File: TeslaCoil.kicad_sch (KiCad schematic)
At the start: 12 parts, among them J1 USB_B_Micro, J2 Conn_01x06_Pin, SW1 SW_DPDT_x2, U1 ATtiny25-20S

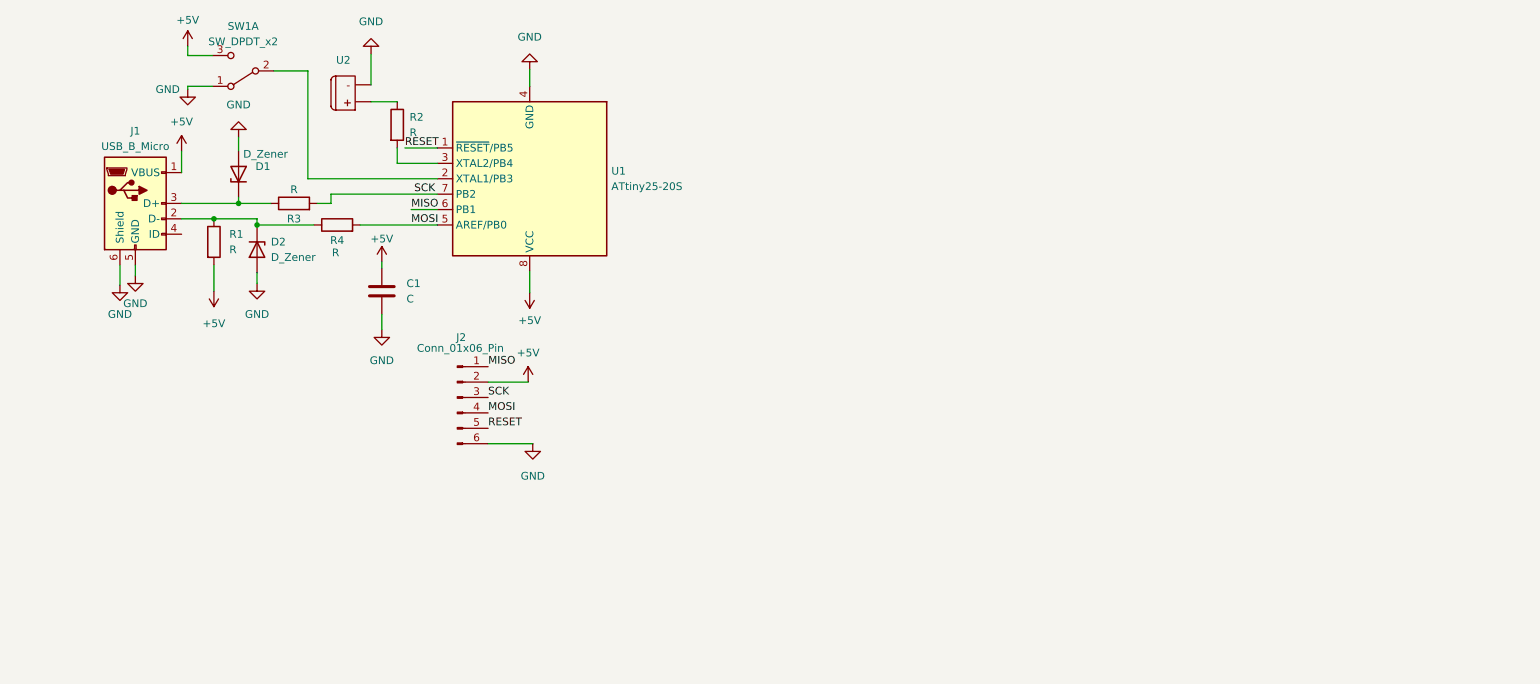
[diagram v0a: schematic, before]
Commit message: Added gitignore, removed backups from version control
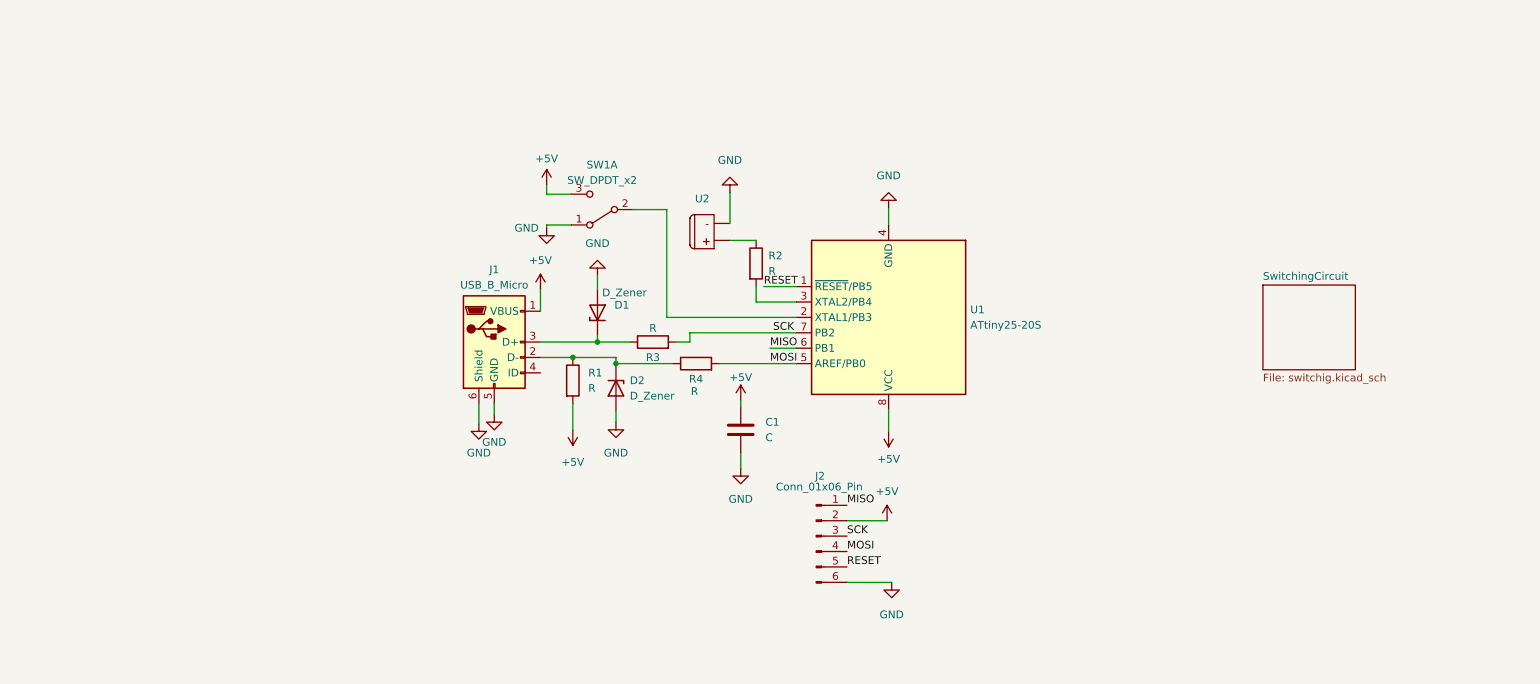
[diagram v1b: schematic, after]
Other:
- added sheet SwitchingCircuit (switchig.kicad_sch)
- company: (none) -> UN Sede Manizales
- title: (none) -> USB Interrupter
- moved on the sheet: C1, D1, D2, J1, J2, R1, R2, R3, R4, SW1A, U1, U2

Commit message: footprints added
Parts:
- C1: value C -> 1u; footprint (none) -> Capacitor_SMD:C_1206_3216Metric
- D1, D2: footprint (none) -> Diode_SMD:D_0603_1608Metric
- R1: value R -> 1.5k; footprint (none) -> Resistor_SMD:R_0402_1005Metric
- R2: value R -> 100; footprint (none) -> Resistor_SMD:R_0402_1005Metric
- R3, R4: value R -> 68; footprint (none) -> Resistor_SMD:R_0402_1005Metric
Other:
- moved on the sheet: D2, J2, R2, R4

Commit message: New project
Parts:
- removed C1: 1u, Capacitor_SMD:C_1206_3216Metric, symbol Device:C
- removed D1, D2: D_Zener, Diode_SMD:D_0603_1608Metric, symbol Device:D_Zener
- removed J1: USB_B_Micro, Connector_USB:USB_Micro-B_Molex-105017-0001, symbol Connector:USB_B_Micro
- removed J2: Conn_01x06_Pin, Connector_PinHeader_1.00mm:PinHeader_2x03_P1.00mm_Vertical, symbol Connector:Conn_01x06_Pin
- removed R1: 1.5k, Resistor_SMD:R_0402_1005Metric, symbol Device:R
- removed R2: 100, Resistor_SMD:R_0402_1005Metric, symbol Device:R
- removed R3, R4: 68, Resistor_SMD:R_0402_1005Metric, symbol Device:R
- removed SW1: SW_DPDT_x2, symbol Switch:SW_DPDT_x2
- removed U1: ATtiny25-20S, Package_SO:SOIC-8W_5.3x5.3mm_P1.27mm, symbol MCU_Microchip_ATtiny:ATtiny25-20S
- removed U2: ~, symbol FibreOpticTransmitterJack:FibreOpticTransmitterJack

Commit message: PCB teslacoil
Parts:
- added C1, C2, C3, C4: 1u, Capacitor_SMD:C_1206_3216Metric, symbol Device:C
- added C5, C6, C9: 100u, Capacitor_SMD:C_1206_3216Metric, symbol Device:C_Polarized_US
- added C7, C8: 47u, Capacitor_THT:CP_Radial_D10.0mm_P5.00mm, symbol Device:C_Polarized_US
- added D1, D2: D, Diode_SMD:D_0603_1608Metric, symbol Device:D
- added D3: DF005s, Diode_THT:Diode_Bridge_DIP-4_W7.62mm_P5.08mm, symbol Diode_Bridge:DF005M
- added D4: DF206S-G, Diode_THT:Diode_Bridge_DIP-4_W7.62mm_P5.08mm, symbol Diode_Bridge:DF005M
- added F1: 4A, Fuse:Fuseholder_Clip-6.3x32mm_Littelfuse_102_122_Inline_P34.21x7.62mm_D1.98mm_Horizontal, symbol Device:Fuse
- added J1: Conn_01x03_Pin, Connector_PinHeader_2.54mm:PinHeader_1x03_P2.54mm_Horizontal, symbol Connector:Conn_01x03_Pin
- added J2: Conn_02x02_Counter_Clockwise, Connector_PinHeader_1.00mm:PinHeader_2x02_P1.00mm_Vertical, symbol Connector_Generic:Conn_02x02_Counter_Clockwise
- added J3: Conn_01x03_Pin, Connector_PinHeader_1.00mm:PinHeader_1x03_P1.00mm_Vertical, symbol Connector:Conn_01x03_Pin
- added Q1, Q2: ~, Package_TO_SOT_THT:TO-220-3_Vertical, symbol TeslaCoil:STGB19NC60KDT4
- added R1: 4.7, Resistor_SMD:R_0402_1005Metric, symbol Device:R_US
- added R2: 100K, Resistor_SMD:R_0402_1005Metric, symbol Device:R_US
- added R3: 100k, Resistor_SMD:R_0402_1005Metric, symbol Device:R_US
- added T1: Transformer_1P_1S, TeslaCoil_JDG:AS3010-U-0100-120-S, symbol Device:Transformer_1P_1S
- added T2: ~, TeslaCoil_JDG:PA2002NL, symbol TeslaCoil:PA2002NL
- added U1: ~, TeslaCoil_JDG:SN74LVC2G14-Q1, symbol TeslaCoil:SN74LVC2G14-Q1
- added U2: ~, TeslaCoil_JDG:IF-D95T, symbol TeslaCoil:IF-D95T
- added U3: ~, TeslaCoil_JDG:UCC27425, symbol TeslaCoil:UCC27425
- added U4: 7815L, TeslaCoil_JDG:L7805ABD2T-TR, symbol Regulator_Linear:L7815
- added U5: 78L05Z, TeslaCoil_JDG:L7805ABD2T-TR, symbol Regulator_Linear:L7815
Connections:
- new net: C4.1, U3.7 (OUTA)
- new net: C4.2, J2.3 (Pin_3)
- new net: D3.3, T1.3 (SA)
- new net: D3.4, T1.4 (SB)
- new net: C7.1, D4.1 (+), Q1.2, R2.1
- new net: C7.2, C8.1, J3.3 (Pin_3), R2.2, R3.1
- new net: U2.2 (OUT), U3.1 (ENBA), U3.8 (ENBB)
- new net: U1.4 (2Y), U3.2 (INA), U3.4 (INB)
- new net: R1.1, U3.5 (OUTB)
- new net: J2.1 (Pin_1), R1.2
- new net: J2.2 (Pin_2), T2.8
- new net: J2.4 (Pin_4), T2.1
- new net: J3.1 (Pin_1), Q1.3, Q2.2, T2.3
- new net: Q2.1, T2.4
- new net: C8.2, D4.2 (-), Q2.3, R3.2, T2.5
- new net: Q1.1, T2.6
- new net: D4.4, F1.1
- new net: U1.3 (2A), U1.6 (1Y)
- new net +15V: C3.1, C6.1, U3.6 (VCC), U4.3 (OUT)
- new net +5V: C1.1, C2.1, C9.1, D1.1 (K), U1.5 (VCC), U2.1 (VCC), U5.3 (OUT)
- new net ANT: D1.2 (A), D2.1 (K), J3.2 (Pin_2), U1.1 (1A)
- new net GND: C1.2, C2.2, C3.2, C5.2, C6.2, C9.2, D2.2 (A), D3.2 (-), J1.2 (Pin_2), U1.2 (GND), U2.3 (GND), U3.3 (GND), U4.2 (GND), U5.2 (GND)
- new net HOT: D4.3, J1.1 (Pin_1), T1.1 (AA)
- new net NTRL: F1.2, J1.3 (Pin_3), T1.2 (AB)
- new net VOUT: C5.1, D3.1 (+), U4.1 (IN), U5.1 (IN)
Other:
- removed sheet SwitchingCircuit
- note added: "Antena de retrolimentacion"
- note added: "Conector a la red"

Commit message: TeslaCoild pcb progress
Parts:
- D3, D4: footprint Diode_THT:Diode_Bridge_DIP-4_W7.62mm_P5.08mm -> Diode_SMD:Diode_Bridge_Vishay_DFS
- Q1, Q2: footprint Package_TO_SOT_THT:TO-220-3_Vertical -> TeslaCoil_JDG:STGB19NC60KDT4
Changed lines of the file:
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@@
       (effects (font (size 1.27 1.27)))
     )
-    (property "Footprint" "Package_TO_SOT_THT:TO-220-3_Vertical" (at 212.852 117.094 0)
+    (property "Footprint" "TeslaCoil_JDG:STGB19NC60KDT4" (at 212.852 117.094 0)
       (effects (font (size 1.27 1.27)) hide)
     )
@@
       (effects (font (size 1.27 1.27)))
     )
-    (property "Footprint" "Diode_THT:Diode_Bridge_DIP-4_W7.62mm_P5.08mm" (at 257.937 105.664 0)
+    (property "Footprint" "Diode_SMD:Diode_Bridge_Vishay_DFS" (at 257.937 105.664 0)
       (effects (font (size 1.27 1.27)) (justify left) hide)
     )
-    (property "Datasheet" "http://www.vishay.com/docs/88571/dfm.pdf" (at 261.112 109.474 0)
+    (property "Datasheet" "https://www.mouser.com/datasheet/2/80/QW_BBR47_DF2005S_G_Thru__DF210S_G_RevG-3083826.pdf" (at 261.112 109.474 0)
       (effects (font (size 1.27 1.27)) hide)
     )
@@
       (effects (font (size 1.27 1.27)))
     )
-    (property "Footprint" "Diode_THT:Diode_Bridge_DIP-4_W7.62mm_P5.08mm" (at 163.322 61.849 0)
+    (property "Footprint" "Diode_SMD:Diode_Bridge_Vishay_DFS" (at 163.322 61.849 0)
       (effects (font (size 1.27 1.27)) (justify left) hide)
     )
-    (property "Datasheet" "http://www.vishay.com/docs/88571/dfm.pdf" (at 159.512 65.024 0)
+    (property "Datasheet" "https://www.vishay.com/docs/88573/dfs.pdf" (at 159.512 65.024 0)
       (effects (font (size 1.27 1.27)) hide)
     )
@@
       (effects (font (size 1.27 1.27)))
     )
-    (property "Footprint" "Package_TO_SOT_THT:TO-220-3_Vertical" (at 212.852 104.394 0)
-      (effects (font (size 1.27 1.27)) hide)
-    )
+    (property "Footprint" "TeslaCoil_JDG:STGB19NC60KDT4" (at 212.852 104.394 0)
+      (effects (font (size 1.27 1.27)) hide)
+    )

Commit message: Final PCB
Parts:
- J1: footprint Connector_PinHeader_2.54mm:PinHeader_1x03_P2.54mm_Horizontal -> Connector_Wire:SolderWire-0.5sqmm_1x03_P4.6mm_D0.9mm_OD2.1mm_Relief
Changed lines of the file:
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@@
       (effects (font (size 1.27 1.27)))
     )
-    (property "Footprint" "Connector_PinHeader_2.54mm:PinHeader_1x03_P2.54mm_Horizontal" (at 71.882 56.134 0)
+    (property "Footprint" "Connector_Wire:SolderWire-0.5sqmm_1x03_P4.6mm_D0.9mm_OD2.1mm_Relief" (at 71.882 56.134 0)
       (effects (font (size 1.27 1.27)) hide)
     )
-    (property "Datasheet" "https://www.lcsc.com/product-detail/Pin-Headers_span-style-background-color-ff0-ZHOURI-span-PZ2-54-1-3_C5360899.html" (at 71.882 56.134 0)
+    (property "Datasheet" "" (at 71.882 56.134 0)
       (effects (font (size 1.27 1.27)) hide)
     )
